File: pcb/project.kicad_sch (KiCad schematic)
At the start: 5 parts, among them J1 USB_B_Micro, U1 RP2040, U2 NCP1117-3.3_SOT223

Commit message: Implemented circuit
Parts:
- removed J1: USB_B_Micro, symbol Connector:USB_B_Micro
- removed U1: RP2040, Package_DFN_QFN:QFN-56-1EP_7x7mm_P0.4mm_EP3.2x3.2mm, symbol MCU_RaspberryPi:RP2040
- removed U2: NCP1117-3.3_SOT223, Package_TO_SOT_SMD:SOT-223-3_TabPin2, symbol Regulator_Linear:NCP1117-3.3_SOT223
- added D1: 1N5822, Diode_SMD:D_0603_1608Metric, symbol Diode:1N5822
- added J1: Pi Pico Headers 1-20, Connector_PinSocket_2.54mm:PinSocket_1x20_P2.54mm_Vertical, symbol Connector_Generic:Conn_01x20
- added J2: Pi Pico Headers 21-40, Connector_PinSocket_2.54mm:PinSocket_1x20_P2.54mm_Vertical, symbol Connector_Generic:Conn_01x20
- added J3: 12v Wall Power, Connector_JST:JST_PH_B2B-PH-K_1x02_P2.00mm_Vertical, symbol Connector_Generic:Conn_01x02
- added J4: Reader/NeoPixel, Connector_JST:JST_PH_B8B-PH-K_1x08_P2.00mm_Vertical, symbol Connector_Generic:Conn_01x08
- added J5: 12v Door Lock, Connector_JST:JST_PH_B2B-PH-K_1x02_P2.00mm_Vertical, symbol Connector_Generic:Conn_01x02
- added L1: 100 uH, Inductor_SMD:L_0603_1608Metric, symbol Device:L
- added Q1: Door Switch, Package_TO_SOT_SMD:SOT-23, symbol Transistor_FET:DMN2040U
- added U1: LM2576S-5, Package_TO_SOT_SMD:TO-263-5_TabPin3, symbol Regulator_Switching:LM2576S-5
- C1: value 10u -> 100uF; footprint (none) -> Capacitor_SMD:C_0603_1608Metric
- C2: value 10u -> 1000uF; footprint (none) -> Capacitor_SMD:C_0603_1608Metric
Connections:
- net +3.3V: now also J2.16 (Pin_16); no longer C2.1
- net GND: now also D1.2 (A), J1.13 (Pin_13), J1.18 (Pin_18), J1.3 (Pin_3), J1.8 (Pin_8), J2.13 (Pin_13), J2.18 (Pin_18), J2.3 (Pin_3), J2.8 (Pin_8), J3.1 (Pin_1), J4.2 (Pin_2), J5.1 (Pin_1), U1.3 (GND), U1.5 (~{ON}/OFF)
- net VBUS renamed +12V
- net +12V: now also J3.2 (Pin_2), Q1.2 (S), U1.1 (VIN)
- new net: J1.1 (Pin_1), J4.3 (Pin_3)
- new net: J1.2 (Pin_2), J4.4 (Pin_4)
- new net: J1.4 (Pin_4), J4.5 (Pin_5)
- new net: J1.5 (Pin_5), J4.6 (Pin_6)
- new net: J1.6 (Pin_6), J4.7 (Pin_7)
- new net: J2.9 (Pin_9), Q1.1 (G)
- new net: J5.2 (Pin_2), Q1.3 (D)
- new net: D1.1 (K), L1.1, U1.2 (OUT)
- new net +5V: C2.1, J2.19 (Pin_19), J4.1 (Pin_1), L1.2, U1.4 (FB)
- no-connect marks 1 -> 24

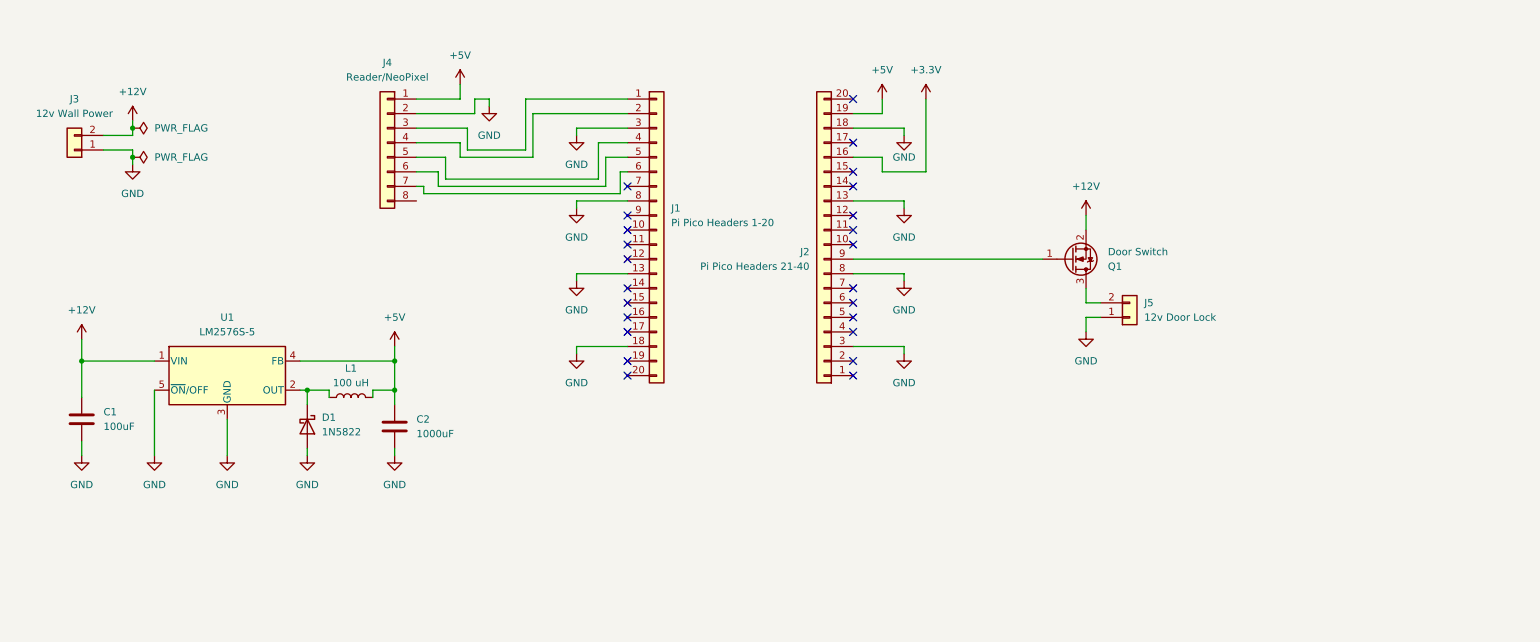
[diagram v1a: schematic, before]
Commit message: Update schematic with feedback
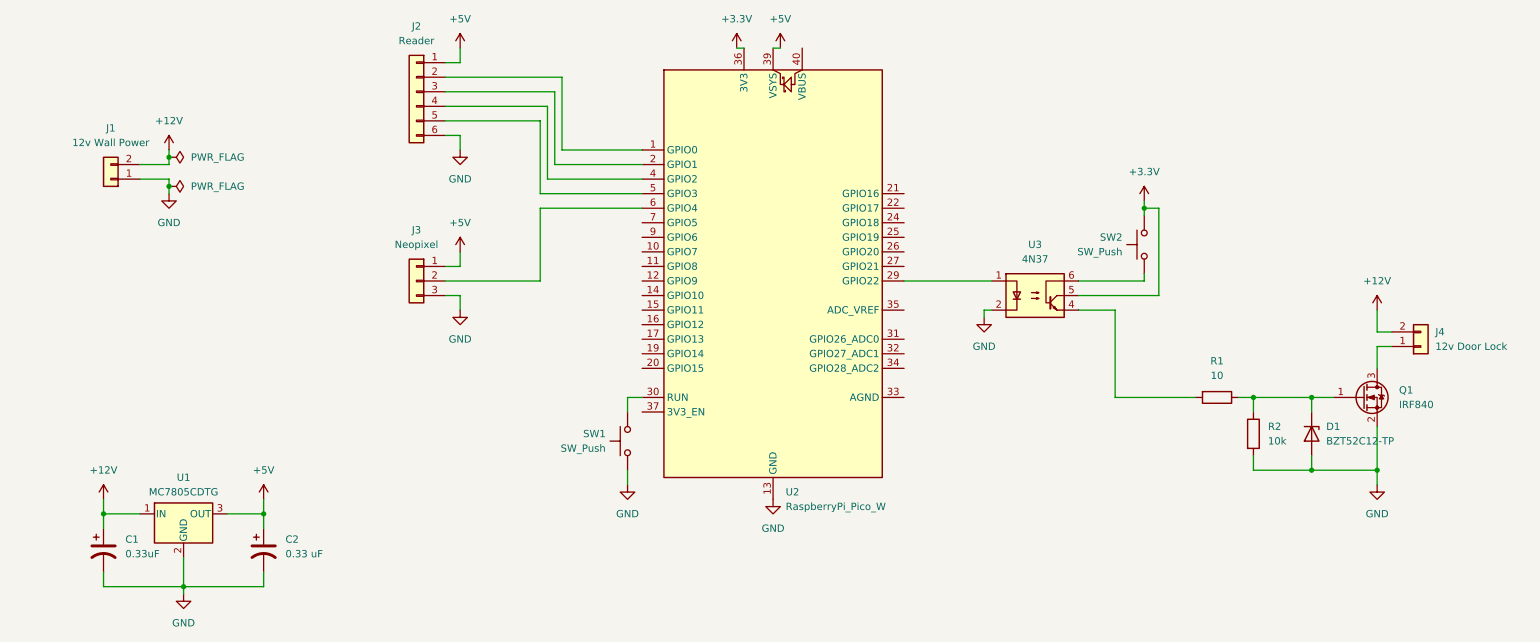
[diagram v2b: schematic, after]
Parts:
- removed C1: 100uF, Capacitor_SMD:C_0603_1608Metric, symbol Device:C
- removed C2: 1000uF, Capacitor_SMD:C_0603_1608Metric, symbol Device:C
- removed D1: 1N5822, Diode_SMD:D_0603_1608Metric, symbol Diode:1N5822
- removed J1: Pi Pico Headers 1-20, Connector_PinSocket_2.54mm:PinSocket_1x20_P2.54mm_Vertical, symbol Connector_Generic:Conn_01x20
- removed J2: Pi Pico Headers 21-40, Connector_PinSocket_2.54mm:PinSocket_1x20_P2.54mm_Vertical, symbol Connector_Generic:Conn_01x20
- removed J4: Reader/NeoPixel, Connector_JST:JST_PH_B8B-PH-K_1x08_P2.00mm_Vertical, symbol Connector_Generic:Conn_01x08
- removed L1: 100 uH, Inductor_SMD:L_0603_1608Metric, symbol Device:L
- removed U1: LM2576S-5, Package_TO_SOT_SMD:TO-263-5_TabPin3, symbol Regulator_Switching:LM2576S-5
- added C1: 0.33uF, Capacitor_THT:CP_Radial_D5.0mm_P2.00mm, symbol Device:C_Polarized_US
- added C2: 0.33 uF, Capacitor_THT:CP_Radial_D5.0mm_P2.00mm, symbol Device:C_Polarized_US
- added D1: BZT52C12-TP, Diode_SMD:D_SOD-123, symbol Device:D_Zener
- added J2: Reader, Connector_JST:JST_PH_B6B-PH-K_1x06_P2.00mm_Vertical, symbol Connector_Generic:Conn_01x06
- added J3: Neopixel, Connector_JST:JST_PH_B3B-PH-K_1x03_P2.00mm_Vertical, symbol Connector_Generic:Conn_01x03
- added R1: 10, Resistor_SMD:R_0603_1608Metric, symbol Device:R
- added R2: 10k, Resistor_SMD:R_0603_1608Metric, symbol Device:R
- added SW1, SW2: SW_Push, symbol Switch:SW_Push
- added U1: MC7805CDTG, Package_TO_SOT_SMD:TO-252-2, symbol Regulator_Linear:L7805
- added U2: RaspberryPi_Pico_W, Module_RaspberryPi_Pico:RaspberryPi_Pico_Common, symbol MCU_Module_RaspberryPi_Pico:RaspberryPi_Pico_W
- added U3: 4N37, Package_DIP:DIP-6_W7.62mm, symbol Isolator:4N37
- Q1: value Door Switch -> IRF840; footprint Package_TO_SOT_SMD:SOT-23 -> Package_TO_SOT_THT:TO-220-3_Horizontal_TabDown
- renumbered J3 to J1, J5 to J4
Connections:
- net +12V: now also J4.2 (Pin_2), C1.1, U1.1 (IN); no longer Q1.2 (S)
- net +3.3V: now also SW2.1, U2.36 (3V3), U3.5
- net +5V: now also C2.1, J2.1 (Pin_1), J3.1 (Pin_1), U1.3 (OUT), U2.39 (VSYS)
- net GND: now also Q1.2 (S), C1.2, C2.2, D1.2 (A), J2.6 (Pin_6), J3.3 (Pin_3), R2.2, SW1.2, U1.2 (GND), U2.13 (GND), U2.18 (GND), U2.23 (GND), U2.28 (GND), U2.3 (GND), U2.38 (GND), U2.8 (GND), U3.2; no longer J4.1 (Pin_1)
- net at Q1.1 (G): now also D1.1 (K), R1.1, R2.1
- net at Q1.3 (D): now also J4.1 (Pin_1); no longer J4.2 (Pin_2)
- new net: U2.29 (GPIO22), U3.1
- new net: R1.2, U3.4
- new net: SW2.2, U3.6
- new net: J3.2 (Pin_2), U2.6 (GPIO4)
- new net: J2.2 (Pin_2), U2.1 (GPIO0)
- new net: J2.3 (Pin_3), U2.2 (GPIO1)
- new net: SW1.1, U2.30 (RUN)
- new net: J2.4 (Pin_4), U2.4 (GPIO2)
- new net: J2.5 (Pin_5), U2.5 (GPIO3)
- no-connect marks 24 -> 0
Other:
- moved on the sheet: J1, J4, Q1

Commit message: Updated PCB
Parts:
- D1: value BZT52C12-TP -> 1N5242BTR; footprint Diode_SMD:D_SOD-123 -> Diode_THT:D_A-405_P7.62mm_Horizontal
- R1, R2: footprint Resistor_SMD:R_0603_1608Metric -> Resistor_THT:R_Axial_DIN0207_L6.3mm_D2.5mm_P10.16mm_Horizontal
- SW1, SW2: footprint (none) -> Button_Switch_THT:SW_PUSH_6mm
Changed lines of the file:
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@@
 			)
 		)
-		(property "Value" "BZT52C12-TP"
+		(property "Value" " 1N5242BTR"
 			(at 251.46 96.52 90)
 			(effects
@@
 			)
 		)
-		(property "Footprint" "Diode_SMD:D_SOD-123"
+		(property "Footprint" "Diode_THT:D_A-405_P7.62mm_Horizontal"
 			(at 248.92 95.25 0)
 			(effects
@@
 			)
 		)
-		(property "Datasheet" "https://www.mccsemi.com/pdf/Products/BZT52C2V4~BZT52C75(500mW)(SOD-123).pdf"
+		(property "Datasheet" "https://www.mouser.com/datasheet/2/308/1N5221B_D-2309445.pdf"
 			(at 248.92 95.25 0)
 			(effects
@@
 			)
 		)
-		(property "Footprint" ""
+		(property "Footprint" "Button_Switch_THT:SW_PUSH_6mm"
 			(at 214.63 62.23 0)
 			(effects
@@
 			)
 		)
-		(property "Footprint" "Resistor_SMD:R_0603_1608Metric"
+		(property "Footprint" "Resistor_THT:R_Axial_DIN0207_L6.3mm_D2.5mm_P10.16mm_Horizontal"
 			(at 232.41 87.122 90)
 			(effects
@@
 			)
 		)
-		(property "Footprint" ""
+		(property "Footprint" "Button_Switch_THT:SW_PUSH_6mm"
 			(at 124.46 96.52 0)
 			(effects
@@
 			)
 		)
-		(property "Footprint" "Resistor_SMD:R_0603_1608Metric"
+		(property "Footprint" "Resistor_THT:R_Axial_DIN0207_L6.3mm_D2.5mm_P10.16mm_Horizontal"
 			(at 236.982 95.25 90)
 			(effects
